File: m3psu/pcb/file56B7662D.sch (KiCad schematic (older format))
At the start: 6 parts

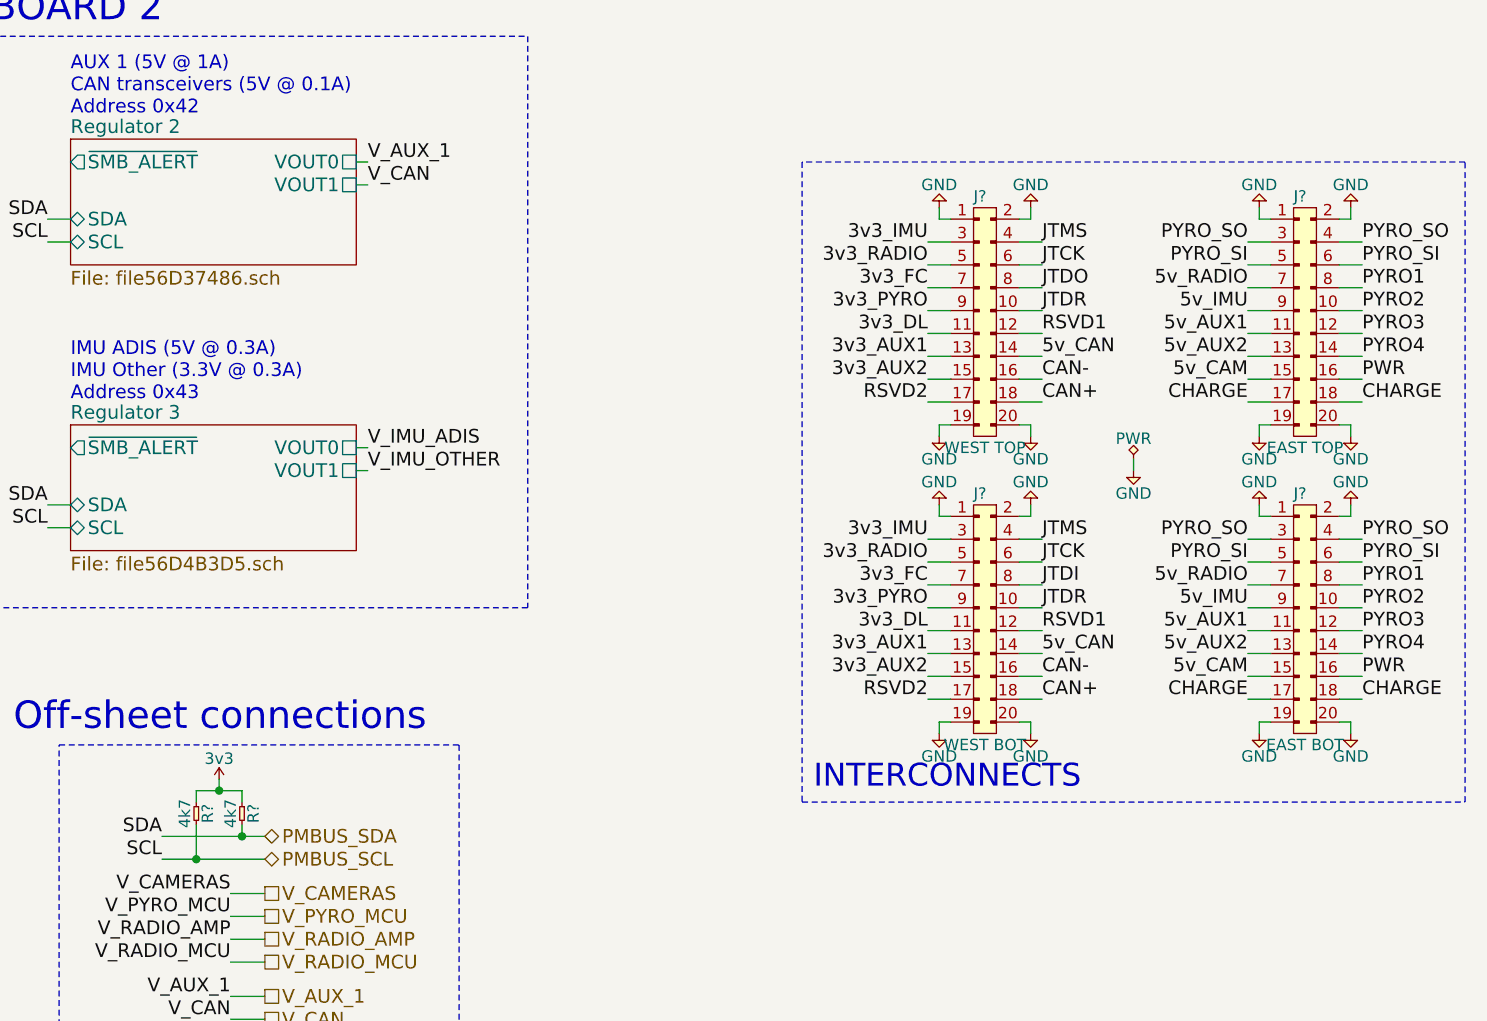
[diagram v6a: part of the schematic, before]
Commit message: Changes to Li-ion charger, north local interconnect.
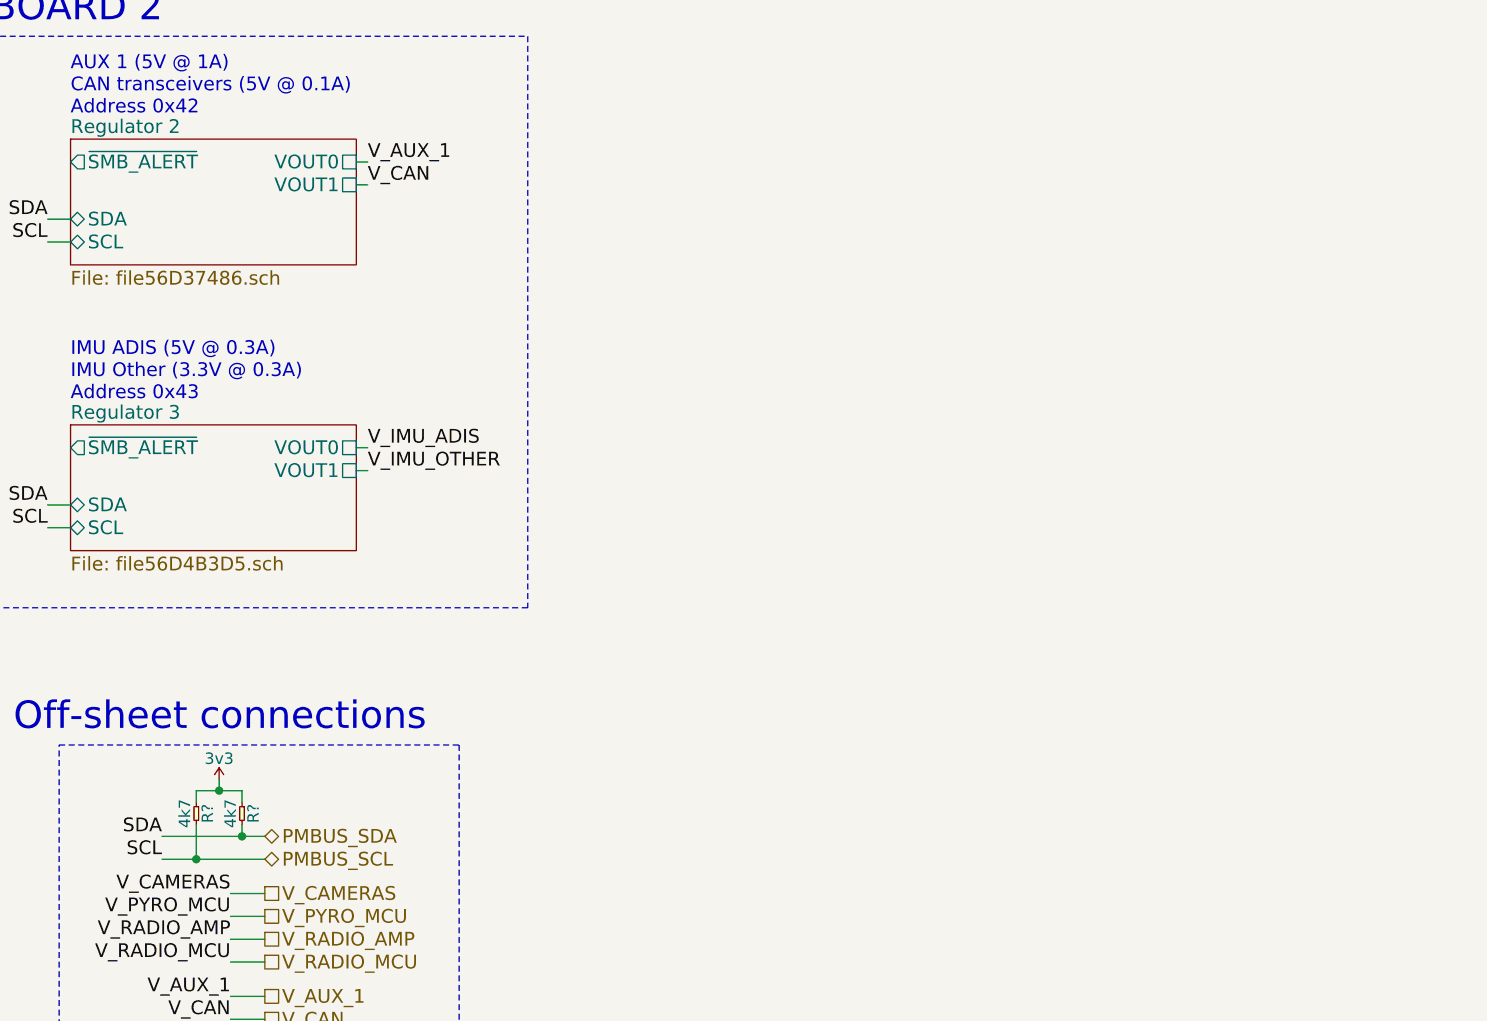
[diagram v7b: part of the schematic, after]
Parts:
- removed J?: WEST TOP, symbol CONN_02x10
- removed J?: EAST TOP, symbol CONN_02x10
- removed J?: WEST BOT, symbol CONN_02x10
- removed J?: EAST BOT, symbol CONN_02x10
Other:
- note removed: "INTERCONNECTS"

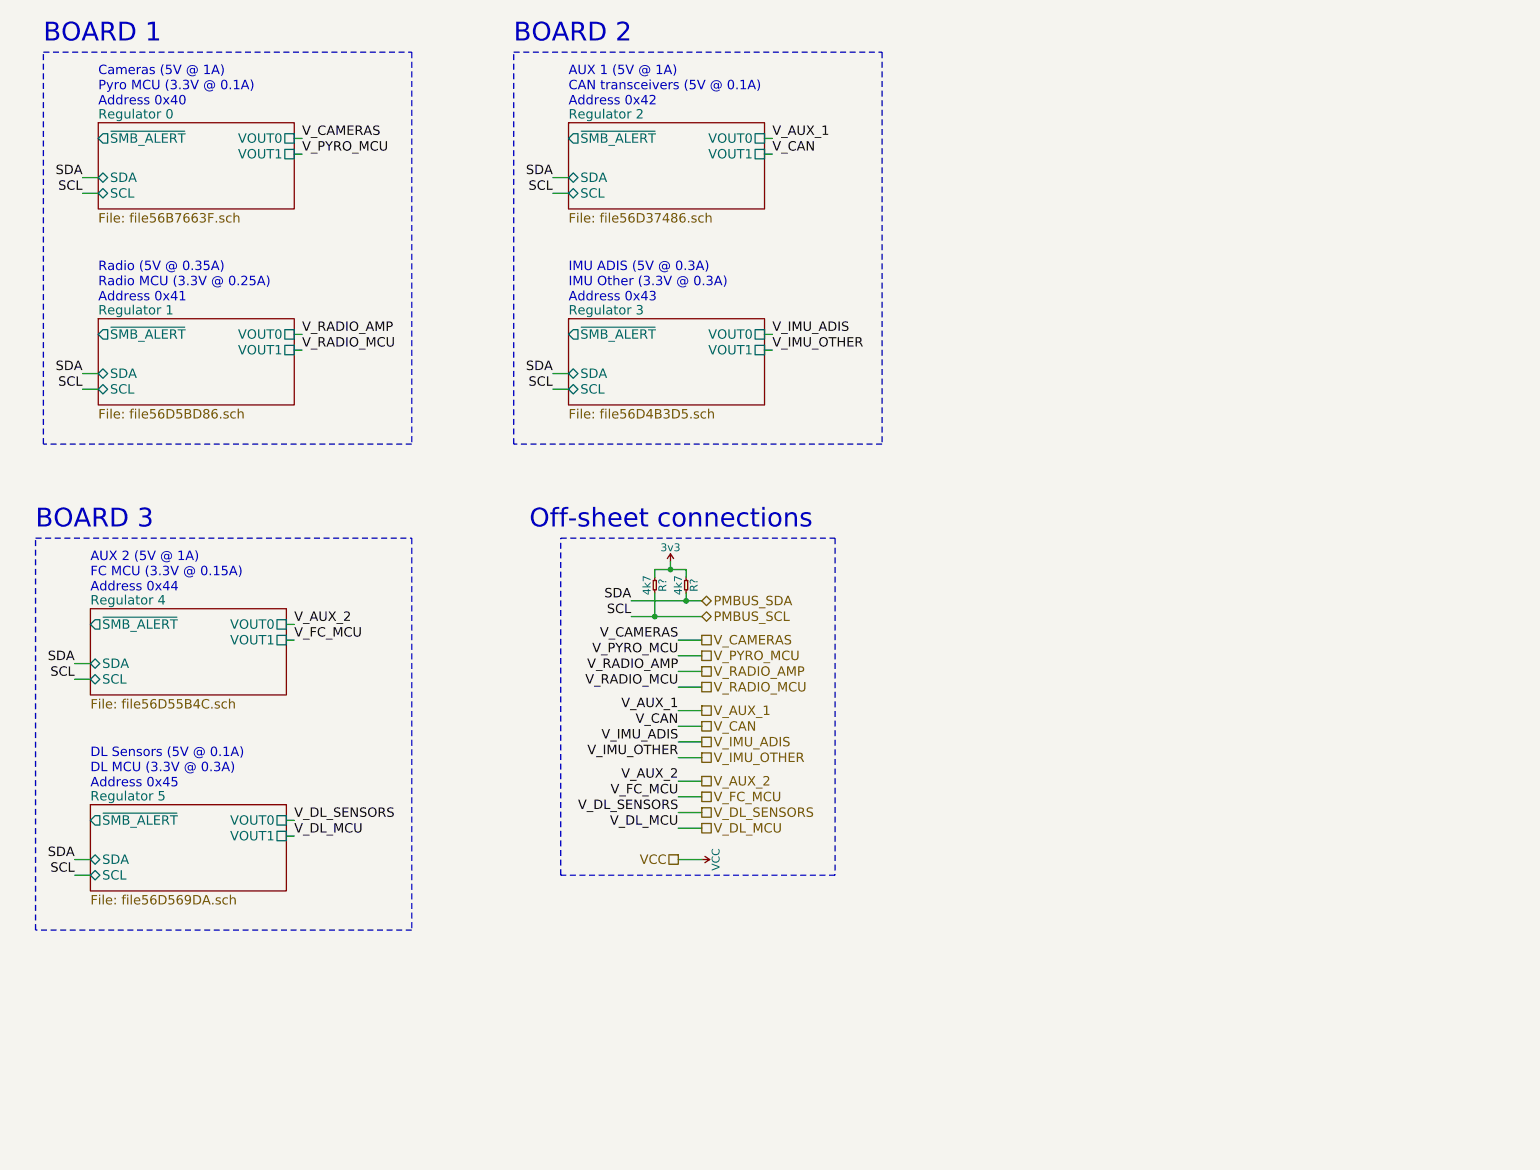
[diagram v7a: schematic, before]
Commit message: Grouped components, sorted internal interconnects. Sheets size now roughly proportional to number of components inside.
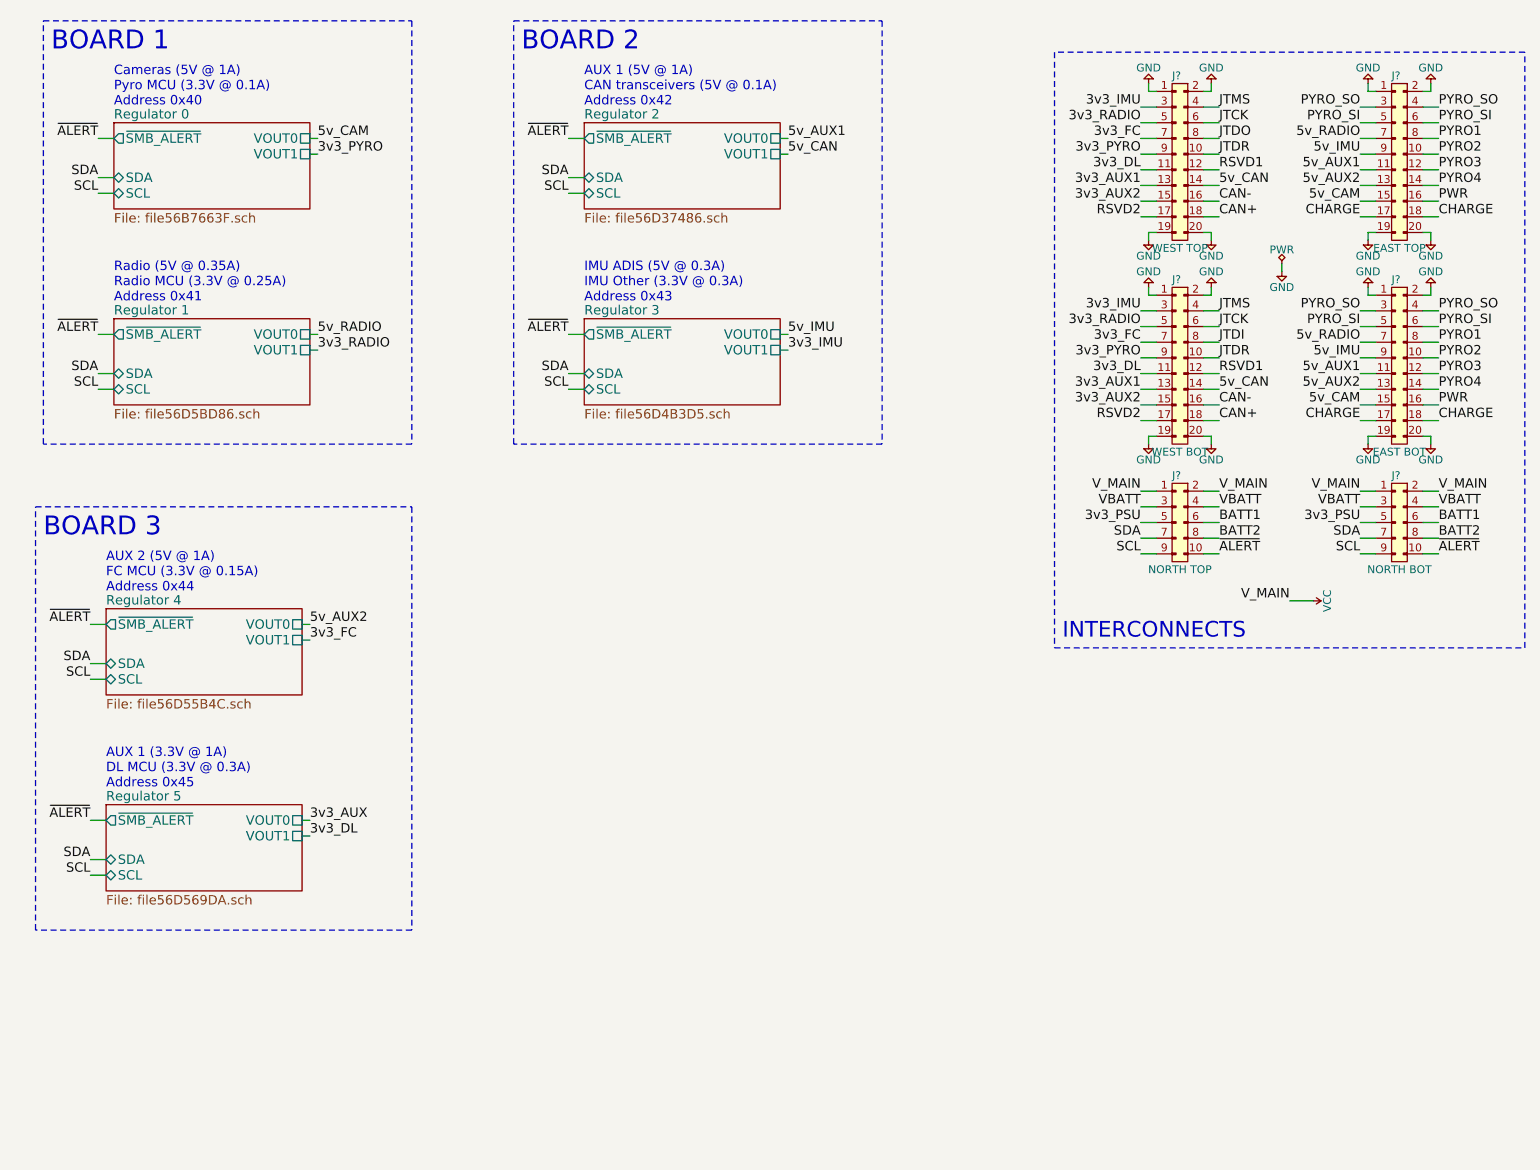
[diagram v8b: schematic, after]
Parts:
- removed R? (x2): 4k7, agg:0402, symbol R
- added J?: WEST TOP, symbol CONN_02x10
- added J?: EAST TOP, symbol CONN_02x10
- added J?: WEST BOT, symbol CONN_02x10
- added J?: EAST BOT, symbol CONN_02x10
- added J?: NORTH TOP, symbol CONN_02x05
- added J?: NORTH BOT, symbol CONN_02x05
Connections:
- net VCC: now also J?.1, J?.1, J?.2, J?.2
- new net 3v3_AUX1: J?.13, J?.13
- new net 3v3_AUX2: J?.15, J?.15
- new net 3v3_DL: J?.11, J?.11
- new net 3v3_FC: J?.7, J?.7
- new net 3v3_IMU: J?.3, J?.3
- new net 3v3_PSU: J?.5, J?.5
- new net 3v3_PYRO: J?.9, J?.9
- new net 3v3_RADIO: J?.5, J?.5
- new net 5v_AUX1: J?.11, J?.11
- new net 5v_AUX2: J?.13, J?.13
- new net 5v_CAM: J?.15, J?.15
- new net 5v_CAN: J?.14, J?.14
- new net 5v_IMU: J?.9, J?.9
- new net 5v_RADIO: J?.7, J?.7
- new net BATT1: J?.6, J?.6
- new net BATT2: J?.8, J?.8
- new net CAN+: J?.18, J?.18
- new net CAN-: J?.16, J?.16
- new net CHARGE: J?.17, J?.17, J?.18, J?.18
- new net GND: J?.1, J?.1, J?.1, J?.1, J?.19, J?.19, J?.19, J?.19, J?.2, J?.2, J?.2, J?.2, J?.20, J?.20, J?.20, J?.20
- new net JTCK: J?.6, J?.6
- new net JTDI: J?.8
- new net JTDO: J?.8
- new net JTDR: J?.10, J?.10
- new net JTMS: J?.4, J?.4
- new net PWR: J?.16, J?.16
- new net PYRO1: J?.8, J?.8
- new net PYRO2: J?.10, J?.10
- new net PYRO3: J?.12, J?.12
- new net PYRO4: J?.14, J?.14
- new net PYRO_SI: J?.5, J?.5, J?.6, J?.6
- new net PYRO_SO: J?.3, J?.3, J?.4, J?.4
- new net RSVD1: J?.12, J?.12
- new net RSVD2: J?.17, J?.17
- new net SCL: J?.9, J?.9
- new net SDA: J?.7, J?.7
- new net VBATT: J?.3, J?.3, J?.4, J?.4
- new net ~ALERT: J?.10, J?.10
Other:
- note added: "AUX 1 (3.3V @ 1A)\nDL MCU (3.3V @ 0.3A)\nAddress 0x45"
- note added: "INTERCONNECTS"
- note removed: "DL Sensors (5V @ 0.1A)\nDL MCU (3.3V @ 0.3A)\nAddress 0x45"
- note removed: "Off-sheet connections"
